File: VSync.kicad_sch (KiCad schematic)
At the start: 12 parts, among them U12 74LS30, U13 74LS30, U15 74LS00, U2 74LS30, U25 74LS161, U26 74LS161, U27 74LS161, U28 74LS04, U29 74LS04, U3 74LS30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

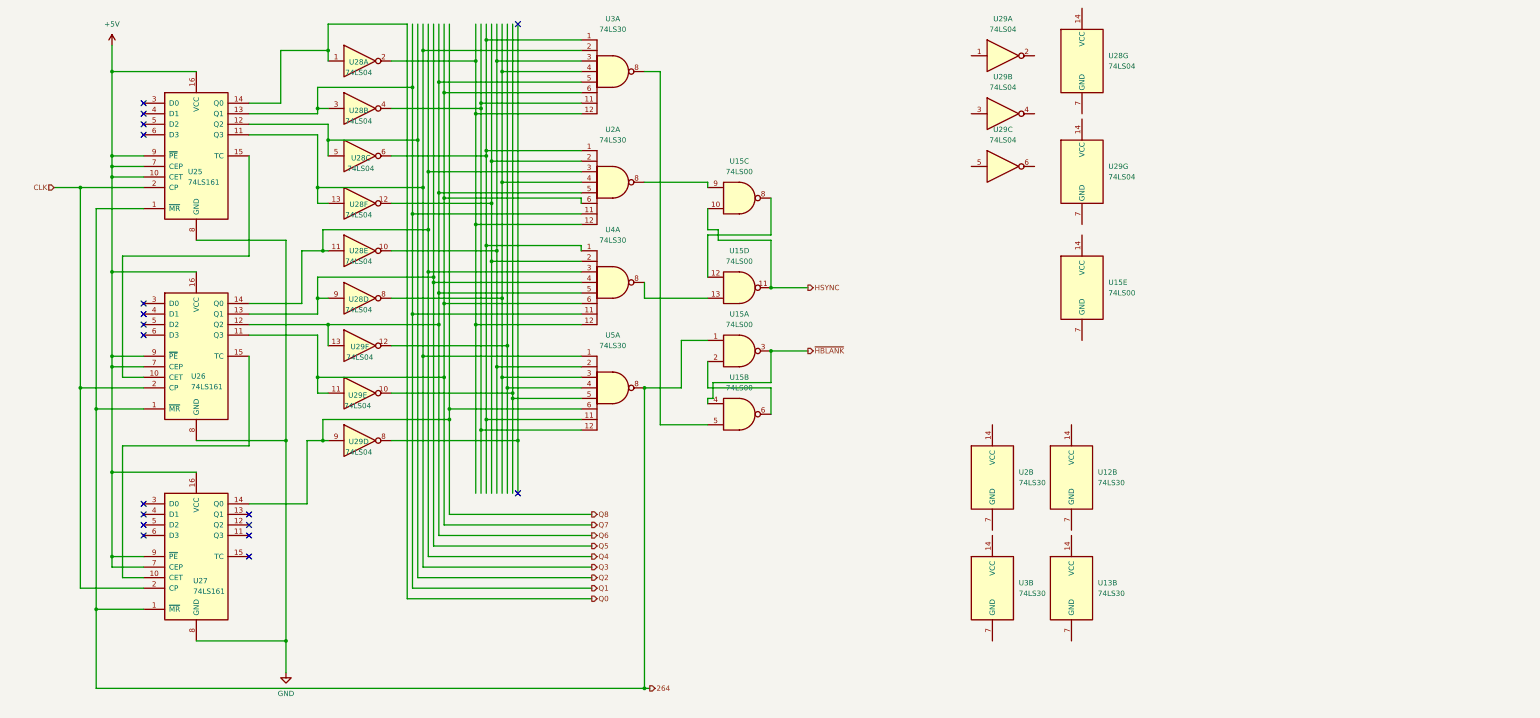
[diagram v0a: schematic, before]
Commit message: Set up schematic for Vertical Sync circit.
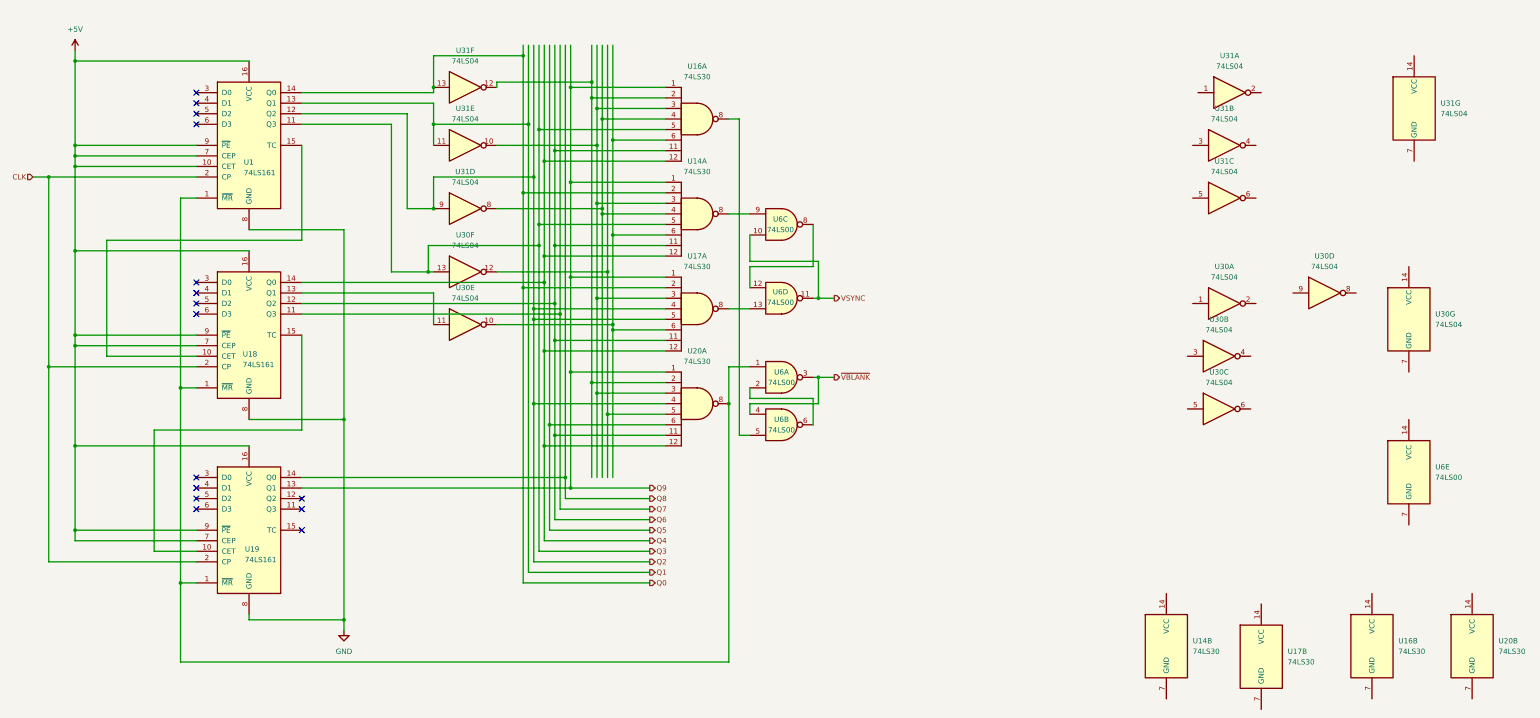
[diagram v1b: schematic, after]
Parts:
- removed U12, U13, U2, U3, U4, U5: 74LS30, symbol 74xx:74LS30
- removed U15: 74LS00, symbol 74xx:74LS00
- removed U25, U26, U27: 74LS161, symbol 74xx:74LS161
- removed U28, U29: 74LS04, symbol 74xx:74LS04
- added U1, U18, U19: 74LS161, symbol 74xx:74LS161
- added U14, U16, U17, U20: 74LS30, symbol 74xx:74LS30
- added U30, U31: 74LS04, symbol 74xx:74LS04
- added U6: 74LS00, symbol 74xx:74LS00
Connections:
- net +5V: now also U1.10 (CET), U1.16 (VCC), U1.7 (CEP), U1.9 (~{PE}), U18.16 (VCC), U18.7 (CEP), U18.9 (~{PE}), U19.16 (VCC), U19.7 (CEP), U19.9 (~{PE})
- net CLK: now also U1.2 (CP), U18.2 (CP), U19.2 (CP)
- net GND: now also U1.8 (GND), U18.8 (GND), U19.8 (GND)
- net Q0: now also U1.14 (Q0), U14.2, U17.2, U31.13
- net Q1: now also U1.13 (Q1), U31.11
- net Q2: now also U1.12 (Q2), U17.4, U17.5, U20.4, U31.9
- net Q3: now also U1.11 (Q3), U14.5, U16.5, U30.13
- net Q4: now also U14.12, U16.12, U17.12, U18.14 (Q0), U20.12
- net Q5: now also U20.6
- net Q6: now also U14.11, U16.11, U17.11, U18.12 (Q2), U20.11
- net Q7: now also U18.11 (Q3)
- net Q8: now also U19.14 (Q0)
- new net: U1.1 (~{MR}), U18.1 (~{MR}), U19.1 (~{MR}), U20.8, U6.1
- new net: U1.15 (TC), U18.10 (CET)
- new net: U6.12, U6.8
- new net: U14.8, U6.9
- new net: U17.8, U6.13
- new net: U14.3, U16.3, U17.3, U20.3, U31.10
- new net: U14.4, U16.4, U31.8
- new net: U14.6, U16.6, U17.6, U30.10
- new net: U20.5, U30.12
- new net: U16.2, U20.2, U31.12
- new net: U16.8, U6.5
- new net: U6.2, U6.6
- new net: U18.15 (TC), U19.10 (CET)
- new net: U18.13 (Q1), U30.11
- new net Q9: U14.1, U16.1, U17.1, U19.13 (Q1), U20.1
- new net VSYNC: U6.10, U6.11
- new net ~{VBLANK}: U6.3, U6.4
- no-connect marks 18 -> 15
